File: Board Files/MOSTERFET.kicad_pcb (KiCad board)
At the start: 2 copper layers, 50 x 60 mm, 32 parts, among them CN11 Jumper_NC_Small, CN21 Jumper_NC_Small, J11 XT-60, J12 XT-60, J21 XT-60, J22 XT-60, Q11 AUIRFSA8409-7P, Q21 AUIRFSA8409-7P, U11 TLP182, U21 TLP182

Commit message: Fixed footprint reference
Fixed footprint Reference for open harware symbole
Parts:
- removed the REF*** at (80.0, 87.0)
- added LO1: Logo_Open_Hardware_Large, Symbols:OSHW-Symbol_8.9x8mm_SilkScreen, F.Cu at (80.0, 87.0)
- J11, J21: value XT-60 -> XT-60-M
- J12, J22: value XT-60 -> XT-60-F

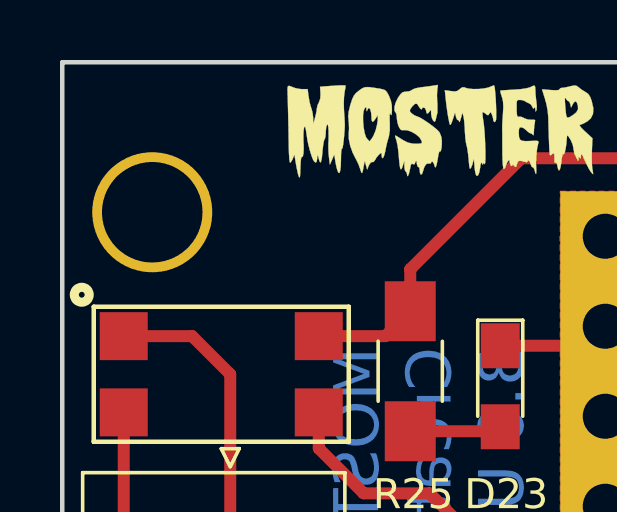
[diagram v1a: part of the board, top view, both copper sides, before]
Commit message: Fixed Errors
Fixed some rendering errors and some placment errors
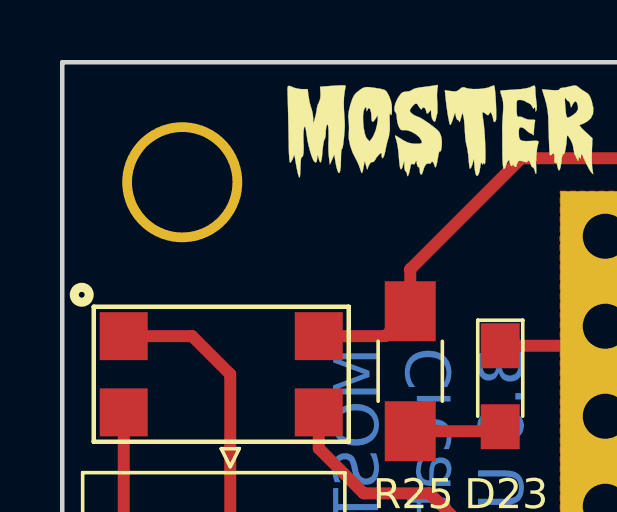
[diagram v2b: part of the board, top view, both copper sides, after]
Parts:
- moved H1 1.41 mm to (77.0, 86.0)
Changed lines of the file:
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@@
       (at (xyz 0 0 0))
       (scale (xyz 1 1 1))
-      (rotate (xyz 0 0 0))
+      (rotate (xyz 0 0 90))
     )
   )
@@
       (at (xyz 0 0 0))
       (scale (xyz 1 1 1))
-      (rotate (xyz 0 0 0))
+      (rotate (xyz 0 0 90))
     )
   )
@@
   )
   (module Mounting_Holes:MountingHole_3.2mm_M3 (layer F.Cu)
-    (at 76 87)
+    (at 77 86)
     (descr "Mounting Hole 3.2mm, no annular, M3")
     (tags "mounting hole 3.2mm no annular m3")

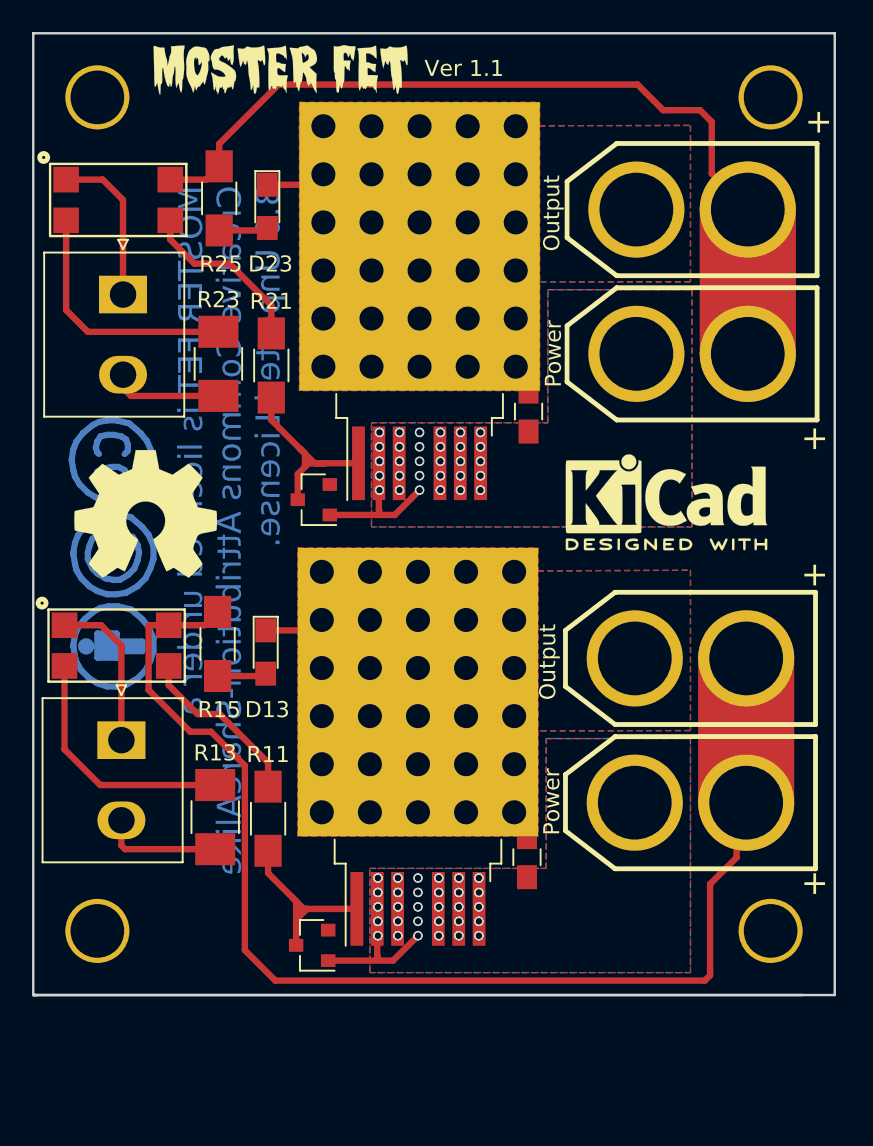
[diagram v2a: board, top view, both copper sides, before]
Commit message: Reduced heat sink size
Reduced heat sink size
Made logo bigger
reduce circuit size
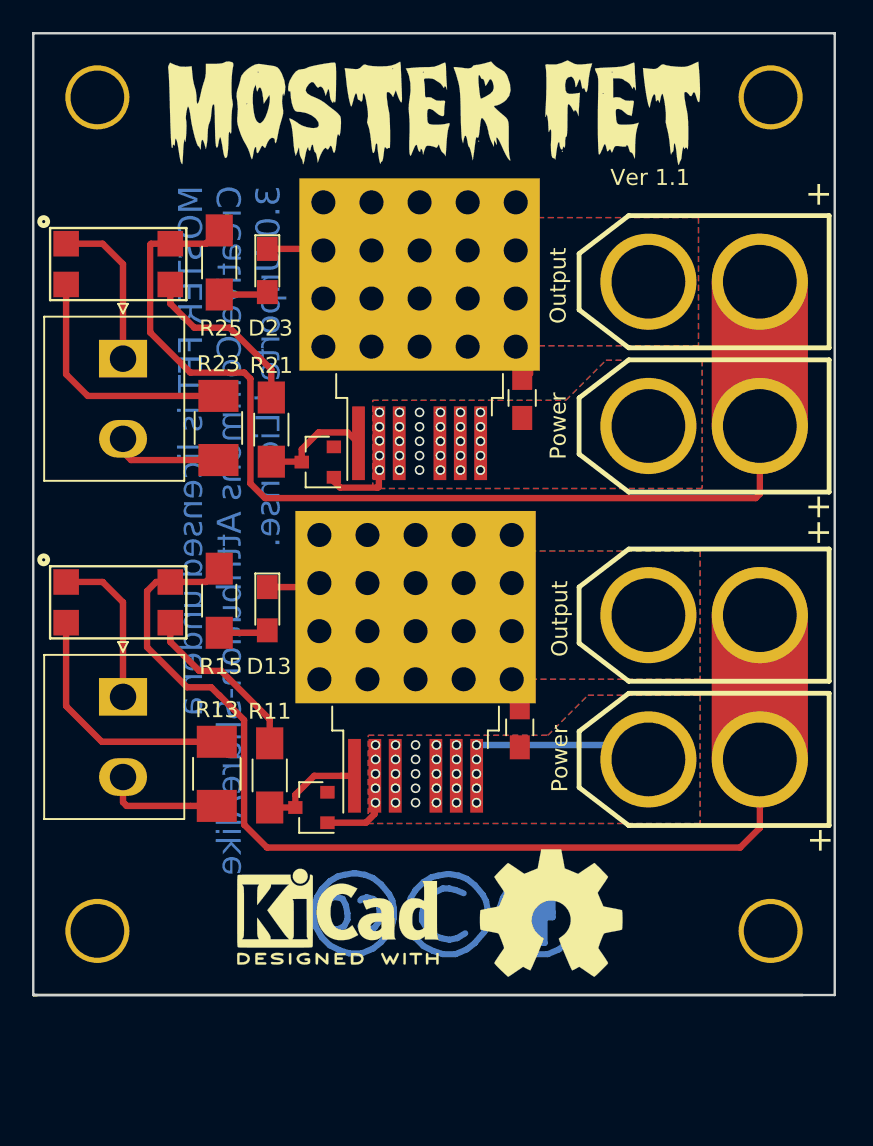
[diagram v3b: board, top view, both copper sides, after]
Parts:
- removed ~: ~, MyLib:MOSTER_FET_LOGO
- added G***: LOGO, MyLib:MOSTER_FET_LOGO_2, F.Cu at (98.0, 62.0)
- Q11, Q21: footprint MyLib:TO-263-6-HeatSunk -> MyLib:TO-263-6-SMALL_HeatSunk
- moved LO1 35.5 mm to (105.3, 111.9)
- moved REF*** 33.0 mm to (92.0, 112.1)
- moved REF** 32.3 mm to (93.2, 112.0), turned to 180 degrees
- moved REF** 31.4 mm to (104.6, 112.0), turned to 180 degrees
- moved REF** 30.6 mm to (98.8, 112.0), turned to 180 degrees
- moved D11 8.60 mm to (90.3, 105.3)
- moved Q11 8.30 mm to (96.8, 97.5)
- moved C11 8.11 mm to (103.3, 100.3)
- moved J21 4.56 mm to (114.8, 81.5)
- moved J22 4.56 mm to (114.8, 72.5)
- moved CN21 4.00 mm to (78.6, 77.3)
- moved D23 4.00 mm to (87.6, 71.8)
- moved R21 4.00 mm to (87.8, 81.7)
- moved R23 4.00 mm to (84.5, 81.6)
- moved R25 4.00 mm to (84.6, 71.3)
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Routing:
- net +BATT: track 132.9 -> 139.9 mm
- net Net-(D21-Pad3): track 12.8 -> 6.96 mm
- net Net-(D11-Pad3): track 12.2 -> 6.58 mm
- net GND: track 18.5 -> 21.3 mm
- net Net-(C21-Pad1): track 5.65 -> 7.00 mm
